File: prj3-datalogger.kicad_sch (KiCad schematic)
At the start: 0 parts

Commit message: have added requred symbols to the schematic sheet.
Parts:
- added BT1: Battery, symbol Device:Battery
- added C1, C2, C3, C4: C, symbol Device:C
- added C5: C_Polarized, symbol Device:C_Polarized
- added D1, D2: LED, symbol Device:LED
- added H1, H2, H3, H4: MountingHole, symbol Mechanical:MountingHole
- added R1, R2, R3, R4: R, symbol Device:R
- added U1, U2: 24LC1025, symbol Memory_EEPROM:24LC1025
- added U3: DS1337S_, DS1337S_:SOIC127P600X175-8N, symbol DS1337S_:DS1337S_
- added U4: ATMEGA328P-AU, ATMEGA328P-AU:QFP80P900X900X120-32N, symbol ATMEGA328P-AU:ATMEGA328P-AU
- added Y1, Y2: Crystal, symbol Device:Crystal
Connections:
- new net GND: U4.21 (GND), U4.3 (GND), U4.5 (GND)
- new net VCC: U4.4 (VCC), U4.6 (VCC)
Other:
- added sheet connectors (connectors.kicad_sch)
- title: (none) -> ${Project_name}

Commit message: arranged symbols.
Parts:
- added R5, R6, R7: R, symbol Device:R
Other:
- moved on the sheet: BT1, C1, C2, C3, C4, C5, D1, D2, R1, R2, R3, R4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

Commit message: added comp values.
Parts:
- C1, C4: value C -> 0.1uF
- C2, C3: value C -> 22pF
- C5: value C_Polarized -> 100nF
- R1, R2: value R -> 330
- R3, R4, R7: value R -> 10K
- R5, R6: value R -> 4.7K
- Y1: value Crystal -> 32.768 KHz
- Y2: value Crystal -> 16 MHz
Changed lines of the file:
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@@
 			)
 		)
-		(property "Value" "Crystal"
+		(property "Value" "16 MHz"
 			(at 191.77 58.4199 90)
 			(show_name no)
@@
 			(at 187.96 57.15 0)
 			(hide yes)
+			(show_name no)
+			(do_not_autoplace no)
+			(effects
+				(font
+					(size 1.27 1.27)
+				)
+			)
+		)
+		(property "Purpose" ""
+			(at 187.96 57.15 0)
 			(show_name no)
 			(do_not_autoplace no)
@@
 			)
 		)
-		(property "Value" "C"
+		(property "Value" "22pF"
 			(at 177.8 55.8799 0)
 			(show_name no)
@@
 			(at 173.99 54.61 0)
 			(hide yes)
+			(show_name no)
+			(do_not_autoplace no)
+			(effects
+				(font
+					(size 1.27 1.27)
+				)
+			)
+		)
+		(property "Purpose" ""
+			(at 173.99 54.61 0)
 			(show_name no)
 			(do_not_autoplace no)
@@
 			)
 		)
-		(property "Value" "C"
+		(property "Value" "0.1uF"
 			(at 184.15 22.86 90)
 			(show_name no)
@@
 			(at 184.15 27.94 0)
 			(hide yes)
+			(show_name no)
+			(do_not_autoplace no)
+			(effects
+				(font
+					(size 1.27 1.27)
+				)
+			)
+		)
+		(property "Purpose" ""
+			(at 184.15 27.94 0)
 			(show_name no)
 			(do_not_autoplace no)
@@
 			)
 		)
-		(property "Value" "C"
+		(property "Value" "22pF"
 			(at 177.8 69.8499 0)
 			(show_name no)
@@
 			(at 173.99 68.58 0)
 			(hide yes)
+			(show_name no)
+			(do_not_autoplace no)
+			(effects
+				(font
+					(size 1.27 1.27)
+				)
+			)
+		)
+		(property "Purpose" ""
+			(at 173.99 68.58 0)
 			(show_name no)
 			(do_not_autoplace no)
@@
 			)
 		)
-		(property "Value" "R"
+		(property "Value" "10K"
 			(at 189.23 74.93 90)
 			(show_name no)
@@
 			(at 189.23 78.74 0)
 			(hide yes)
+			(show_name no)
+			(do_not_autoplace no)
+			(effects
+				(font
+					(size 1.27 1.27)
+				)
+			)
+		)
+		(property "Purpose" ""
+			(at 189.23 78.74 0)
 			(show_name no)
 			(do_not_autoplace no)
@@
 			)
 		)
-		(property "Value" "R"
+		(property "Value" "330"
 			(at 259.08 59.6899 0)
 			(show_name no)
@@
 			(at 256.54 58.42 0)
 			(hide yes)
+			(show_name no)
+			(do_not_autoplace no)
+			(effects
+				(font
+					(size 1.27 1.27)
+				)
+			)
+		)
+		(property "Purpose" ""
+			(at 256.54 58.42 0)
 			(show_name no)
 			(do_not_autoplace no)
@@
 			)
 		)
-		(property "Value" "R"
+		(property "Value" "10K"
 			(at 110.49 45.7199 0)
 			(show_name no)
@@
 			(at 107.95 44.45 0)
 			(hide yes)
+			(show_name no)
+			(do_not_autoplace no)
+			(effects
+				(font
+					(size 1.27 1.27)
+				)
+			)
+		)
+		(property "Purpose" ""
+			(at 107.95 44.45 0)
 			(show_name no)
 			(do_not_autoplace no)
@@
 			)
 		)
-		(property "Value" "R"
+		(property "Value" "330"
 			(at 177.8 39.37 90)
 			(show_name no)
@@
 			(at 177.8 43.18 0)
 			(hide yes)
+			(show_name no)
+			(do_not_autoplace no)
+			(effects
+				(font
+					(size 1.27 1.27)
+				)
+			)
+		)
+		(property "Purpose" ""
+			(at 177.8 43.18 0)
 			(show_name no)
 			(do_not_autoplace no)
@@
 			)
 		)
-		(property "Value" "R"
+		(property "Value" "4.7K"
 			(at 118.11 149.8599 0)
 			(show_name no)
@@
 			(at 115.57 148.59 0)
 			(hide yes)
+			(show_name no)
+			(do_not_autoplace no)
+			(effects
+				(font
+					(size 1.27 1.27)
+				)
+			)
+		)
+		(property "Purpose" ""
+			(at 115.57 148.59 0)
 			(show_name no)
 			(do_not_autoplace no)
@@
 			)
 		)
-		(property "Value" "C"
+		(property "Value" "0.1uF"
 			(at 121.92 45.7199 0)
 			(show_name no)
@@
 			(at 118.11 44.45 0)
 			(hide yes)
+			(show_name no)
+			(do_not_autoplace no)
+			(effects
+				(font
+					(size 1.27 1.27)
+				)
+			)
+		)
+		(property "Purpose" ""
+			(at 118.11 44.45 0)
 			(show_name no)
 			(do_not_autoplace no)
@@
 			)
 		)
-		(property "Value" "C_Polarized"
+		(property "Value" "100nF"
 			(at 250.19 33.4009 0)
 			(show_name no)
@@
 			(at 246.38 33.02 0)
 			(hide yes)
+			(show_name no)
+			(do_not_autoplace no)
+			(effects
+				(font
+					(size 1.27 1.27)
+				)
+			)
+		)
+		(property "Purpose" ""
+			(at 246.38 33.02 0)
 			(show_name no)
 			(do_not_autoplace no)
@@
 			)
 		)
-		(property "Value" "R"
+		(property "Value" "4.7K"
 			(at 106.68 149.8599 0)
 			(show_name no)
@@
 			(at 104.14 148.59 0)
 			(hide yes)
+			(show_name no)
+			(do_not_autoplace no)
+			(effects
+				(font
+					(size 1.27 1.27)
+				)
+			)
+		)
+		(property "Purpose" ""
+			(at 104.14 148.59 0)
 			(show_name no)
 			(do_not_autoplace no)
@@
 			)
 		)
-		(property "Value" "R"
+		(property "Value" "10K"
 			(at 101.6 45.7199 0)
 			(show_name no)
@@
 			(at 99.06 44.45 0)
 			(hide yes)
+			(show_name no)
+			(do_not_autoplace no)
+			(effects
+				(font
+					(size 1.27 1.27)
+				)
+			)
+		)
+		(property "Purpose" ""
+			(at 99.06 44.45 0)
 			(show_name no)
 			(do_not_autoplace no)
@@
 			)
 		)
-		(property "Value" "Crystal"
+		(property "Value" "32.768 KHz"
 			(at 36.83 53.3399 90)
 			(show_name no)
@@
 			(show_name no)
 			(do_not_autoplace no)
+			(effects
+				(font
+					(size 1.27 1.27)
+				)
+			)
+		)
+		(property "Purpose" ""
+			(at 33.02 52.07 0)
+			(show_name no)
+			(do_not_autoplace no)

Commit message: completed symbol-footprint associations.
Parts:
- BT1: footprint (none) -> Connector_PinHeader_2.54mm:PinHeader_1x02_P2.54mm_Vertical
- C1, C2, C3, C4, C5: footprint (none) -> Capacitor_SMD:C_0805_2012Metric
- D1, D2: footprint (none) -> LED_SMD:LED_0805_2012Metric
- H1, H2, H3, H4: footprint (none) -> MountingHole:MountingHole_2.2mm_M2
- R1, R2, R3, R4, R5, R6, R7: footprint (none) -> Resistor_SMD:R_0805_2012Metric
- U1, U2: footprint (none) -> Package_SO:SOIC-8_5.3x5.3mm_P1.27mm
- U3: footprint DS1337S_:SOIC127P600X175-8N -> footprints:SOIC127P600X175-8N
- U4: footprint ATMEGA328P-AU:QFP80P900X900X120-32N -> footprints:QFP80P900X900X120-32N
- Y1, Y2: footprint (none) -> Crystal:Crystal_SMD_5032-2Pin_5.0x3.2mm_HandSoldering
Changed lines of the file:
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@@
 			)
 		)
-		(property "Footprint" ""
+		(property "Footprint" "MountingHole:MountingHole_2.2mm_M2"
 			(at 261.62 148.59 0)
 			(hide yes)
@@
 			)
 		)
-		(property "Footprint" ""
+		(property "Footprint" "Crystal:Crystal_SMD_5032-2Pin_5.0x3.2mm_HandSoldering"
 			(at 187.96 57.15 0)
 			(hide yes)
@@
 			)
 		)
-		(property "Footprint" ""
+		(property "Footprint" "Connector_PinHeader_2.54mm:PinHeader_1x02_P2.54mm_Vertical"
 			(at 262.89 31.496 90)
 			(hide yes)
@@
 			)
 		)
-		(property "Footprint" ""
+		(property "Footprint" "Capacitor_SMD:C_0805_2012Metric"
 			(at 174.9552 58.42 0)
 			(hide yes)
@@
 			)
 		)
-		(property "Footprint" "DS1337S_:SOIC127P600X175-8N"
+		(property "Footprint" "footprints:SOIC127P600X175-8N"
 			(at 72.39 53.34 0)
 			(hide yes)
@@
 			)
 		)
-		(property "Footprint" ""
+		(property "Footprint" "Capacitor_SMD:C_0805_2012Metric"
 			(at 187.96 26.9748 0)
 			(hide yes)
@@
 			)
 		)
-		(property "Footprint" ""
+		(property "Footprint" "Capacitor_SMD:C_0805_2012Metric"
 			(at 174.9552 72.39 0)
 			(hide yes)
@@
 			)
 		)
-		(property "Footprint" ""
+		(property "Footprint" "LED_SMD:LED_0805_2012Metric"
 			(at 256.54 46.99 0)
 			(hide yes)
@@
 			)
 		)
-		(property "Footprint" ""
+		(property "Footprint" "Resistor_SMD:R_0805_2012Metric"
 			(at 189.23 80.518 90)
 			(hide yes)
@@
 			)
 		)
-		(property "Footprint" ""
+		(property "Footprint" "MountingHole:MountingHole_2.2mm_M2"
 			(at 261.62 161.29 0)
 			(hide yes)
@@
 			)
 		)
-		(property "Footprint" ""
+		(property "Footprint" "Package_SO:SOIC-8_5.3x5.3mm_P1.27mm"
 			(at 80.01 148.59 0)
 			(hide yes)
@@
 			)
 		)
-		(property "Footprint" ""
+		(property "Footprint" "MountingHole:MountingHole_2.2mm_M2"
 			(at 261.62 142.24 0)
 			(hide yes)
@@
 			)
 		)
-		(property "Footprint" ""
+		(property "Footprint" "MountingHole:MountingHole_2.2mm_M2"
 			(at 261.62 154.94 0)
 			(hide yes)
@@
 			)
 		)
-		(property "Footprint" ""
+		(property "Footprint" "Resistor_SMD:R_0805_2012Metric"
 			(at 254.762 58.42 90)
 			(hide yes)
@@
 			)
 		)
-		(property "Footprint" ""
+		(property "Footprint" "Package_SO:SOIC-8_5.3x5.3mm_P1.27mm"
 			(at 44.45 148.59 0)
 			(hide yes)
@@
 			)
 		)
-		(property "Footprint" ""
+		(property "Footprint" "Resistor_SMD:R_0805_2012Metric"
 			(at 106.172 44.45 90)
 			(hide yes)
@@
 			)
 		)
-		(property "Footprint" ""
+		(property "Footprint" "Resistor_SMD:R_0805_2012Metric"
 			(at 177.8 44.958 90)
 			(hide yes)
@@
 			)
 		)
-		(property "Footprint" ""
+		(property "Footprint" "Resistor_SMD:R_0805_2012Metric"
 			(at 113.792 148.59 90)
 			(hide yes)
@@
 			)
 		)
-		(property "Footprint" ""
+		(property "Footprint" "Capacitor_SMD:C_0805_2012Metric"
 			(at 119.0752 48.26 0)
 			(hide yes)
@@
 			)
 		)
-		(property "Footprint" "ATMEGA328P-AU:QFP80P900X900X120-32N"
+		(property "Footprint" "footprints:QFP80P900X900X120-32N"
 			(at 219.71 58.42 0)
 			(hide yes)
@@
 			)
 		)
-		(property "Footprint" ""
+		(property "Footprint" "Capacitor_SMD:C_0805_2012Metric"
 			(at 247.3452 36.83 0)
 			(hide yes)
@@
 			)
 		)
-		(property "Footprint" ""
+		(property "Footprint" "Resistor_SMD:R_0805_2012Metric"
 			(at 102.362 148.59 90)
 			(hide yes)
@@
 			)
 		)
-		(property "Footprint" ""
+		(property "Footprint" "Resistor_SMD:R_0805_2012Metric"
 			(at 97.282 44.45 90)
 			(hide yes)
@@
 			)
 		)
-		(property "Footprint" ""
+		(property "Footprint" "Crystal:Crystal_SMD_5032-2Pin_5.0x3.2mm_HandSoldering"
 			(at 33.02 52.07 0)
 			(hide yes)
@@
 			)
 		)
-		(property "Footprint" ""
+		(property "Footprint" "LED_SMD:LED_0805_2012Metric"
 			(at 190.5 43.18 0)
 			(hide yes)

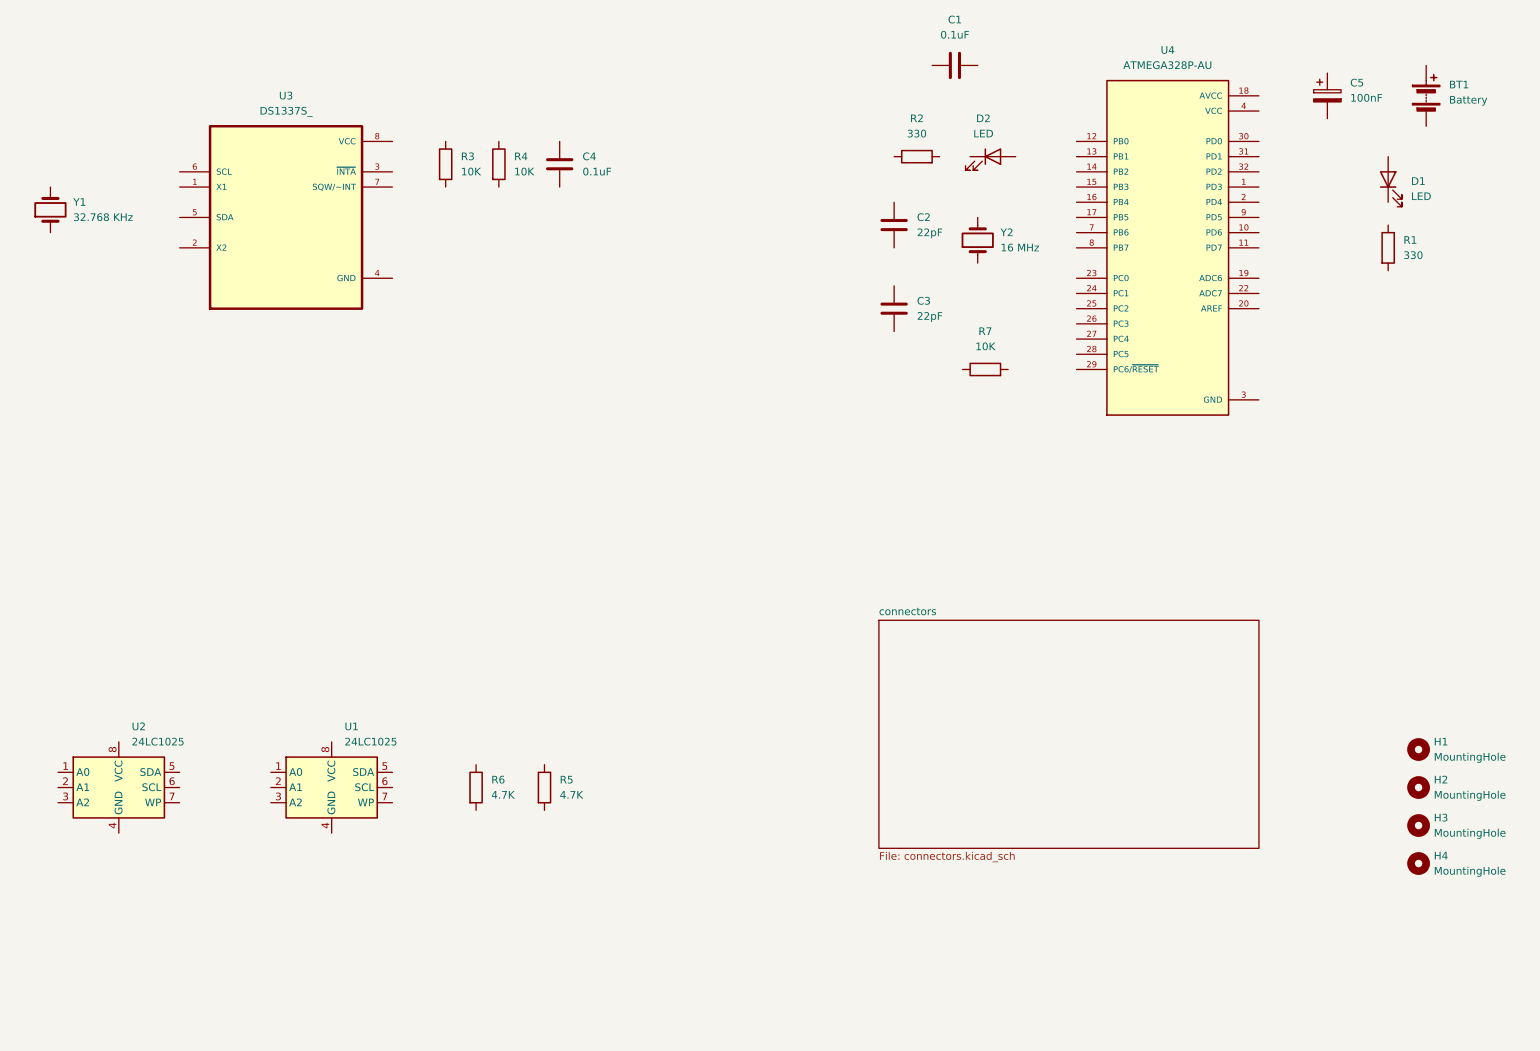
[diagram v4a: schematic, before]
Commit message: completed wiring of main sheet.
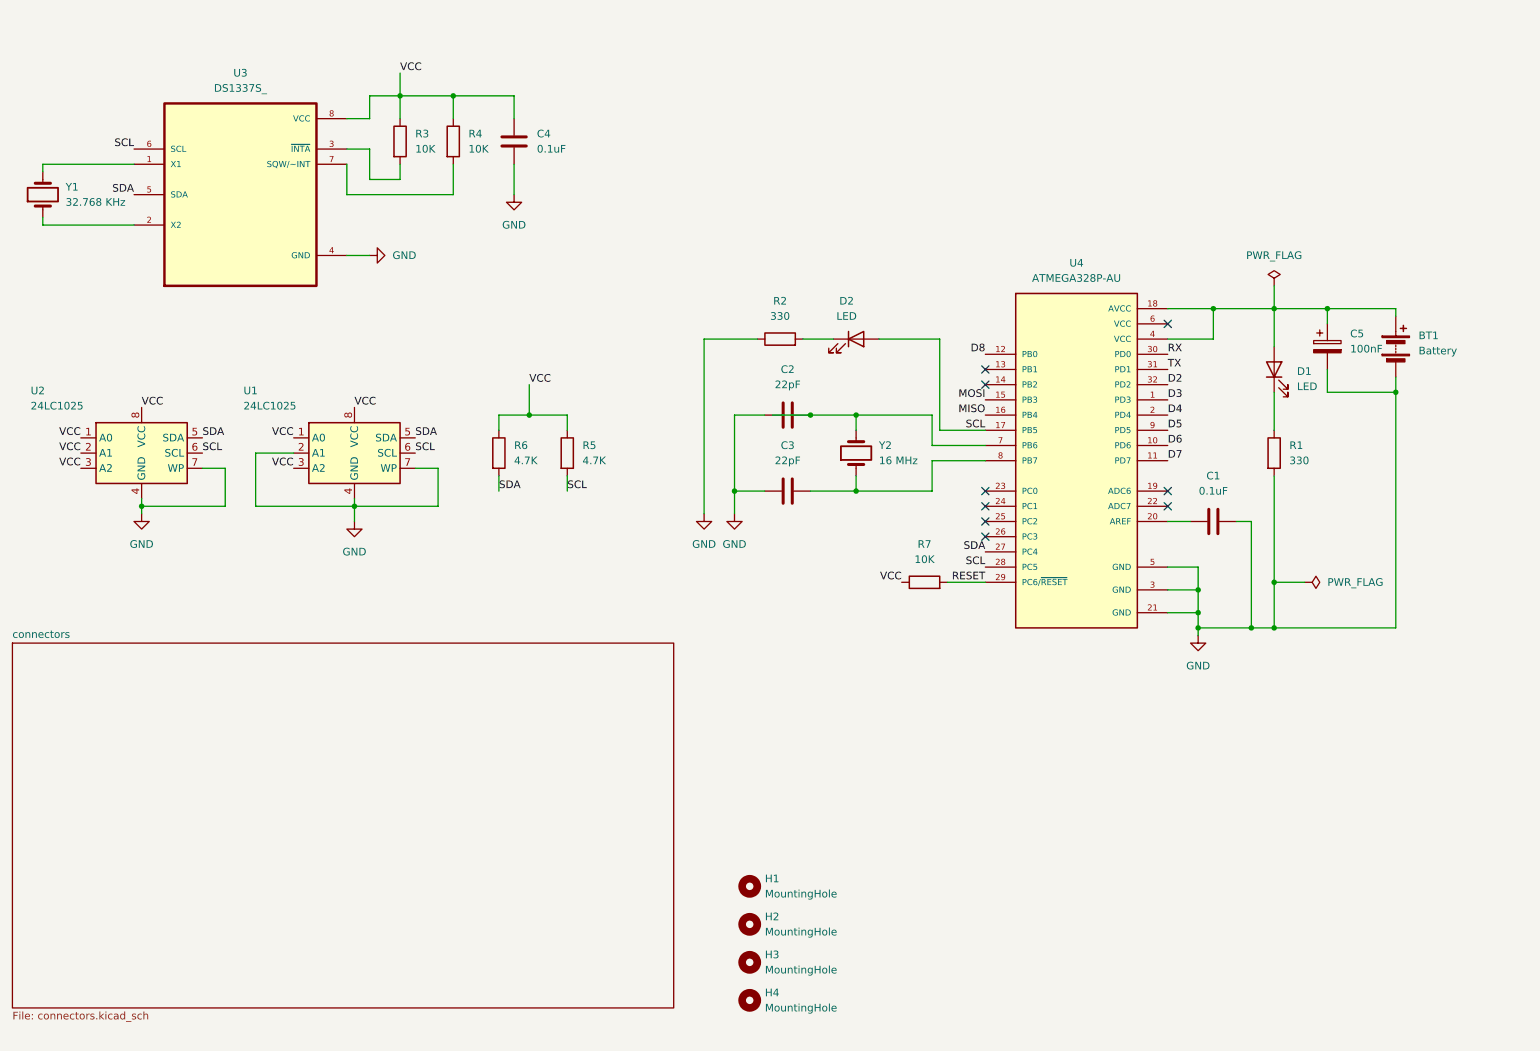
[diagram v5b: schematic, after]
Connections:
- net GND: now also BT1.2 (-), C1.2, C2.1, C3.1, C4.2, C5.2, R1.2, R2.1, U1.2 (A1), U1.4 (GND), U1.7 (WP), U2.4 (GND), U2.7 (WP), U3.4 (GND)
- net VCC: now also C4.1, R3.1, R4.1, R5.1, R6.1, R7.1, U1.1 (A0), U1.3 (A2), U1.8 (VCC), U2.1 (A0), U2.2 (A1), U2.3 (A2), U2.8 (VCC), U3.8 (VCC); no longer U4.4 (VCC), U4.6 (VCC)
- net at Y2.1: now also C3.2, U4.8 (PB7)
- net at Y2.2: now also C2.2, U4.7 (PB6)
- net at BT1.1 (+): now also C5.1, D1.2 (A), U4.18 (AVCC), U4.4 (VCC)
- net at U3.1 (X1): now also Y1.2
- net at U3.2 (X2): now also Y1.1
- net at U3.3 (~{INTA}): now also R3.2
- net SDA: now reaches U3.5 (SDA)
- net SDA: now also R6.2, U1.5 (SDA), U2.5 (SDA), U4.27 (PC4)
- net SCL: now reaches U3.6 (SCL)
- net SCL: now also D2.2 (A), R5.2, U1.6 (SCL), U2.6 (SCL), U4.17 (PB5), U4.28 (PC5)
- net at U3.7 (SQW/~INT): now also R4.2
- net at C1.1: now also U4.20 (AREF)
- net at D1.1 (K): now also R1.1
- net RESET: now reaches R7.2
- net RESET: now also U4.29 (PC6/~{RESET})
- net at R2.2: now also D2.1 (K)
- net D3: now reaches U4.1 (PD3)
- net D6: now reaches U4.10 (PD6)
- net D7: now reaches U4.11 (PD7)
- net D8: now reaches U4.12 (PB0)
- net MOSI: now reaches U4.15 (PB3)
- net MISO: now reaches U4.16 (PB4)
- net D4: now reaches U4.2 (PD4)
- net RX: now reaches U4.30 (PD0)
- net TX: now reaches U4.31 (PD1)
- net D2: now reaches U4.32 (PD2)
- net D5: now reaches U4.9 (PD5)
- no-connect marks 0 -> 9
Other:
- moved on the sheet: BT1, C1, C2, C3, C4, C5, D1, D2, H1, H2, H3, H4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

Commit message: completed wiring in the second sheet.
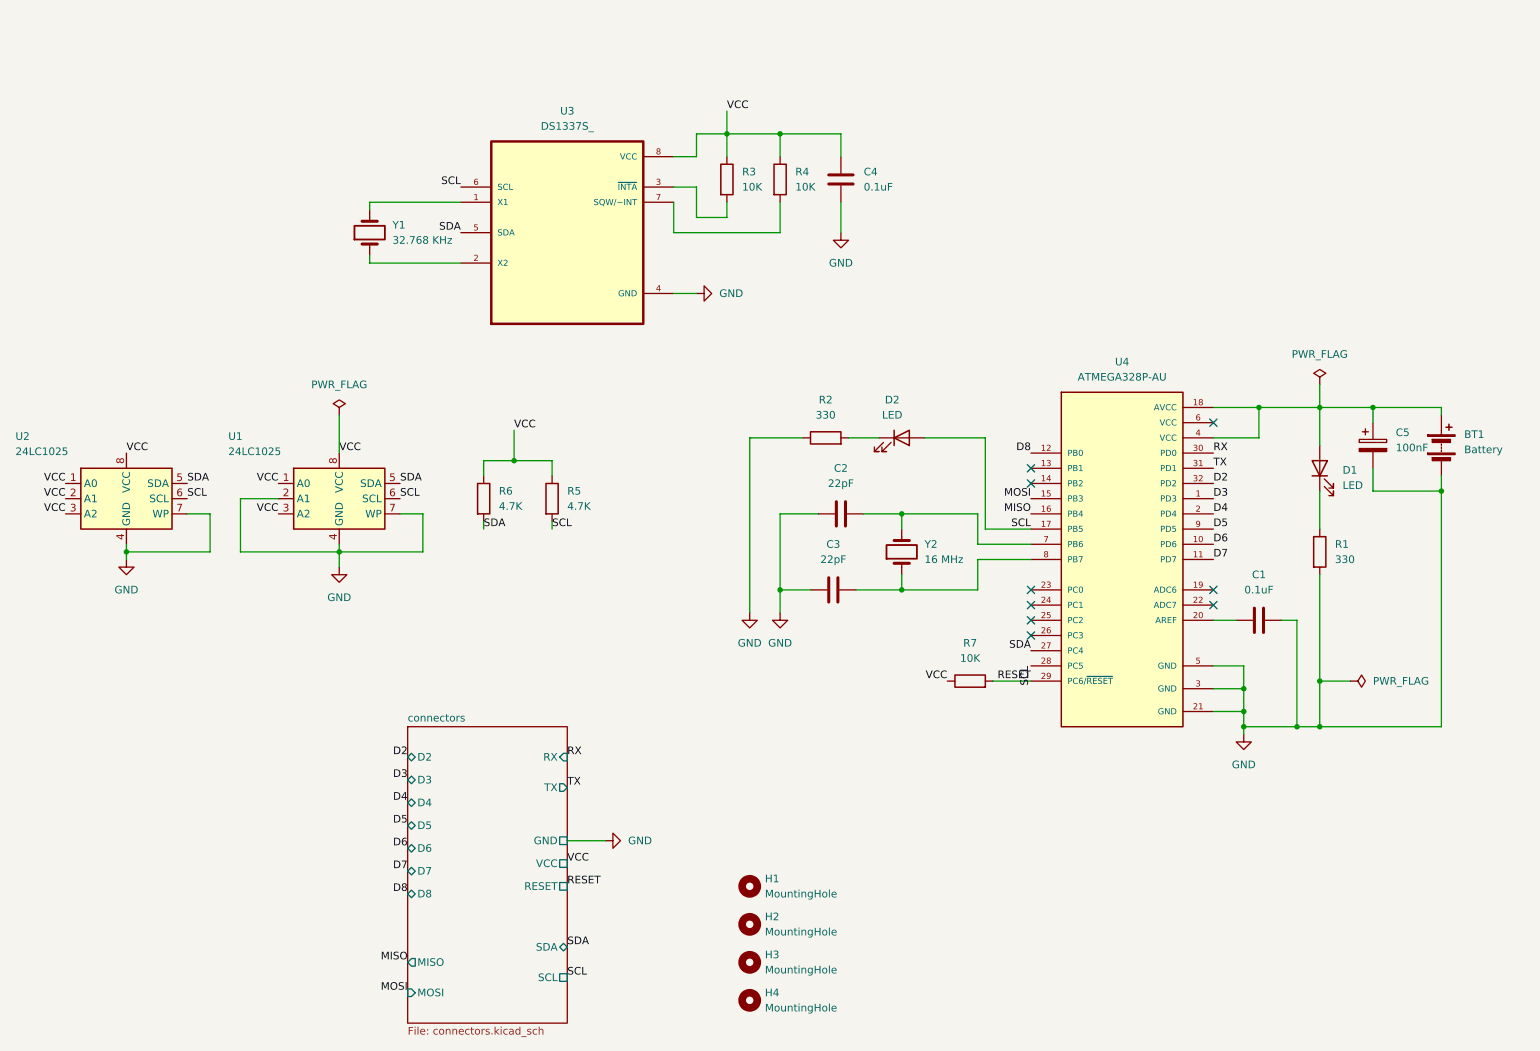
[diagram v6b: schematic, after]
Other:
- sheet connectors ports: added D2, D3, D4, D5, D6, D7, D8, GND, MISO, MOSI, RESET, RX, SCL, SDA, TX, VCC; removed none
- moved on the sheet: BT1, C1, C2, C3, C4, C5, D1, D2, R1, R2, R3, R4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
